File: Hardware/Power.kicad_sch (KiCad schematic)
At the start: 17 parts

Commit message: Replaced the ISOW1044 CAN Transceiver with the ISO1042 + isolated DC-DC and LDO
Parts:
- renumbered C12 to C10, C14 to C11, C16 to C12, C10 to C13, C13 to C14, C17 to C16, C11 to C17
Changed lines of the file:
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@@
 		(on_board yes)
 		(dnp no)
-		(property "Reference" "C14"
+		(property "Reference" "C11"
 			(at 88.9 45.8469 0)
 			(effects
@@
 			(project "CANIO-Board"
 				(path "/a11f98b2-3b09-4cf9-8535-19e509fe91b9/689b7a23-36b5-40a7-9bc7-70c150316ec6"
-					(reference "C14")
+					(reference "C11")
 					(unit 1)
 				)
@@
 		(on_board yes)
 		(dnp no)
-		(property "Reference" "C10"
+		(property "Reference" "C13"
 			(at 27.94 48.3869 0)
 			(effects
@@
 			(project "CANIO-Board"
 				(path "/a11f98b2-3b09-4cf9-8535-19e509fe91b9/689b7a23-36b5-40a7-9bc7-70c150316ec6"
-					(reference "C10")
+					(reference "C13")
 					(unit 1)
 				)
@@
 		(dnp no)
 		(fields_autoplaced yes)
-		(property "Reference" "#PWR09"
+		(property "Reference" "#PWR08"
 			(at 57.15 105.41 0)
 			(effects
@@
 			(project "CANIO-Board"
 				(path "/a11f98b2-3b09-4cf9-8535-19e509fe91b9/689b7a23-36b5-40a7-9bc7-70c150316ec6"
-					(reference "#PWR09")
+					(reference "#PWR08")
 					(unit 1)
 				)
@@
 		(dnp no)
 		(fields_autoplaced yes)
-		(property "Reference" "#FLG03"
+		(property "Reference" "#FLG01"
 			(at 96.52 36.195 0)
 			(effects
@@
 			(project ""
 				(path "/a11f98b2-3b09-4cf9-8535-19e509fe91b9/689b7a23-36b5-40a7-9bc7-70c150316ec6"
-					(reference "#FLG03")
+					(reference "#FLG01")
 					(unit 1)
 				)
@@
 		(dnp no)
 		(fields_autoplaced yes)
-		(property "Reference" "#FLG01"
+		(property "Reference" "#FLG03"
 			(at 39.37 99.695 0)
 			(effects
@@
 			(project "CANIO-Board"
 				(path "/a11f98b2-3b09-4cf9-8535-19e509fe91b9/689b7a23-36b5-40a7-9bc7-70c150316ec6"
-					(reference "#FLG01")
+					(reference "#FLG03")
 					(unit 1)
 				)
@@
 		(dnp no)
 		(fields_autoplaced yes)
-		(property "Reference" "#FLG02"
+		(property "Reference" "#FLG04"
 			(at 73.66 100.965 0)
 			(effects
@@
 			(project "CANIO-Board"
 				(path "/a11f98b2-3b09-4cf9-8535-19e509fe91b9/689b7a23-36b5-40a7-9bc7-70c150316ec6"
-					(reference "#FLG02")
+					(reference "#FLG04")
 					(unit 1)
 				)
@@
 		(on_board yes)
 		(dnp no)
-		(property "Reference" "C11"
+		(property "Reference" "C17"
 			(at 27.94 83.9469 0)
 			(effects
@@
 			(project "CANIO-Board"
 				(path "/a11f98b2-3b09-4cf9-8535-19e509fe91b9/689b7a23-36b5-40a7-9bc7-70c150316ec6"
-					(reference "C11")
+					(reference "C17")
 					(unit 1)
 				)
@@
 		(dnp no)
 		(fields_autoplaced yes)
-		(property "Reference" "#FLG04"
+		(property "Reference" "#FLG02"
 			(at 96.52 71.755 0)
 			(effects
@@
 			(project "CANIO-Board"
 				(path "/a11f98b2-3b09-4cf9-8535-19e509fe91b9/689b7a23-36b5-40a7-9bc7-70c150316ec6"
-					(reference "#FLG04")
+					(reference "#FLG02")
 					(unit 1)
 				)
@@
 		(on_board yes)
 		(dnp no)
-		(property "Reference" "C16"
+		(property "Reference" "C12"
 			(at 99.06 45.8469 0)
 			(effects
@@
 			(project "CANIO-Board"
 				(path "/a11f98b2-3b09-4cf9-8535-19e509fe91b9/689b7a23-36b5-40a7-9bc7-70c150316ec6"
-					(reference "C16")
+					(reference "C12")
 					(unit 1)
 				)
@@
 		(dnp no)
 		(fields_autoplaced yes)
-		(property "Reference" "#PWR05"
+		(property "Reference" "#PWR06"
 			(at 36.83 80.01 0)
 			(effects
@@
 			(project "CANIO-Board"
 				(path "/a11f98b2-3b09-4cf9-8535-19e509fe91b9/689b7a23-36b5-40a7-9bc7-70c150316ec6"
-					(reference "#PWR05")
+					(reference "#PWR06")
 					(unit 1)
 				)
@@
 		(dnp no)
 		(fields_autoplaced yes)
-		(property "Reference" "#PWR010"
+		(property "Reference" "#PWR09"
 			(at 73.66 109.22 0)
 			(effects
@@
 			(project "CANIO-Board"
 				(path "/a11f98b2-3b09-4cf9-8535-19e509fe91b9/689b7a23-36b5-40a7-9bc7-70c150316ec6"
-					(reference "#PWR010")
+					(reference "#PWR09")
 					(unit 1)
 				)
@@
 		(on_board yes)
 		(dnp no)
-		(property "Reference" "C12"
+		(property "Reference" "C10"
 			(at 68.58 40.7669 0)
 			(effects
@@
 			(project "CANIO-Board"
 				(path "/a11f98b2-3b09-4cf9-8535-19e509fe91b9/689b7a23-36b5-40a7-9bc7-70c150316ec6"
-					(reference "C12")
+					(reference "C10")
 					(unit 1)
 				)
@@
 		(on_board yes)
 		(dnp no)
-		(property "Reference" "C13"
+		(property "Reference" "C14"
 			(at 68.58 76.3269 0)
 			(effects
@@
 			(project "CANIO-Board"
 				(path "/a11f98b2-3b09-4cf9-8535-19e509fe91b9/689b7a23-36b5-40a7-9bc7-70c150316ec6"
-					(reference "C13")
+					(reference "C14")
 					(unit 1)
 				)
@@
 		(dnp no)
 		(fields_autoplaced yes)
-		(property "Reference" "#PWR08"
+		(property "Reference" "#PWR010"
 			(at 53.34 199.39 0)
 			(effects
@@
 			(project ""
 				(path "/a11f98b2-3b09-4cf9-8535-19e509fe91b9/689b7a23-36b5-40a7-9bc7-70c150316ec6"
-					(reference "#PWR08")
+					(reference "#PWR010")
 					(unit 1)
 				)
@@
 		(dnp no)
 		(fields_autoplaced yes)
-		(property "Reference" "#PWR06"
+		(property "Reference" "#PWR05"
 			(at 49.53 62.23 0)
 			(effects
@@
 			(project ""
 				(path "/a11f98b2-3b09-4cf9-8535-19e509fe91b9/689b7a23-36b5-40a7-9bc7-70c150316ec6"
-					(reference "#PWR06")
+					(reference "#PWR05")
 					(unit 1)
 				)
@@
 		(on_board yes)
 		(dnp no)
-		(property "Reference" "C17"
+		(property "Reference" "C16"
 			(at 99.06 81.4069 0)
 			(effects
@@
 			(project "CANIO-Board"
 				(path "/a11f98b2-3b09-4cf9-8535-19e509fe91b9/689b7a23-36b5-40a7-9bc7-70c150316ec6"
-					(reference "C17")
-					(unit 1)
-				)
+					(reference "C16")
+					(unit 1)
+				)

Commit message: Replaced G0B1KET6 with KET6N in schematic
- Updated the schematic with new symbol and pinout.
- Updated the rest of the schematic with all resulting changes
	- This includes the 8 output channels, 7 GPIOs, and slightly
	  different WAGO connector configuration.
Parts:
- renumbered C10 to C15, C11 to C16, C12 to C17, C13 to C18, C14 to C19, C15 to C20, C16 to C21, C17 to C22, R8 to R11, R9 to R12
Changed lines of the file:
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@@
 		(on_board yes)
 		(dnp no)
-		(property "Reference" "C11"
+		(property "Reference" "C16"
 			(at 88.9 45.8469 0)
 			(effects
@@
 			(project "CANIO-Board"
 				(path "/a11f98b2-3b09-4cf9-8535-19e509fe91b9/689b7a23-36b5-40a7-9bc7-70c150316ec6"
-					(reference "C11")
+					(reference "C16")
 					(unit 1)
 				)
@@
 		(dnp no)
 		(fields_autoplaced yes)
-		(property "Reference" "#PWR04"
+		(property "Reference" "#PWR05"
 			(at 36.83 44.45 0)
 			(effects
@@
 			(project ""
 				(path "/a11f98b2-3b09-4cf9-8535-19e509fe91b9/689b7a23-36b5-40a7-9bc7-70c150316ec6"
-					(reference "#PWR04")
+					(reference "#PWR05")
 					(unit 1)
 				)
@@
 		(on_board yes)
 		(dnp no)
-		(property "Reference" "C13"
+		(property "Reference" "C18"
 			(at 27.94 48.3869 0)
 			(effects
@@
 			(project "CANIO-Board"
 				(path "/a11f98b2-3b09-4cf9-8535-19e509fe91b9/689b7a23-36b5-40a7-9bc7-70c150316ec6"
-					(reference "C13")
+					(reference "C18")
 					(unit 1)
 				)
@@
 		(dnp no)
 		(fields_autoplaced yes)
-		(property "Reference" "R9"
+		(property "Reference" "R12"
 			(at 77.47 184.15 90)
 			(effects
@@
 			(project "CANIO-Board"
 				(path "/a11f98b2-3b09-4cf9-8535-19e509fe91b9/689b7a23-36b5-40a7-9bc7-70c150316ec6"
-					(reference "R9")
+					(reference "R12")
 					(unit 1)
 				)
@@
 		(dnp no)
 		(fields_autoplaced yes)
-		(property "Reference" "#PWR08"
+		(property "Reference" "#PWR09"
 			(at 57.15 105.41 0)
 			(effects
@@
 			(project "CANIO-Board"
 				(path "/a11f98b2-3b09-4cf9-8535-19e509fe91b9/689b7a23-36b5-40a7-9bc7-70c150316ec6"
-					(reference "#PWR08")
+					(reference "#PWR09")
 					(unit 1)
 				)
@@
 		(dnp no)
 		(fields_autoplaced yes)
-		(property "Reference" "#PWR07"
+		(property "Reference" "#PWR08"
 			(at 49.53 97.79 0)
 			(effects
@@
 			(project "CANIO-Board"
 				(path "/a11f98b2-3b09-4cf9-8535-19e509fe91b9/689b7a23-36b5-40a7-9bc7-70c150316ec6"
-					(reference "#PWR07")
+					(reference "#PWR08")
 					(unit 1)
 				)
@@
 		(on_board yes)
 		(dnp no)
-		(property "Reference" "C17"
+		(property "Reference" "C22"
 			(at 27.94 83.9469 0)
 			(effects
@@
 			(project "CANIO-Board"
 				(path "/a11f98b2-3b09-4cf9-8535-19e509fe91b9/689b7a23-36b5-40a7-9bc7-70c150316ec6"
-					(reference "C17")
+					(reference "C22")
 					(unit 1)
 				)
@@
 		(on_board yes)
 		(dnp no)
-		(property "Reference" "C12"
+		(property "Reference" "C17"
 			(at 99.06 45.8469 0)
 			(effects
@@
 			(project "CANIO-Board"
 				(path "/a11f98b2-3b09-4cf9-8535-19e509fe91b9/689b7a23-36b5-40a7-9bc7-70c150316ec6"
-					(reference "C12")
+					(reference "C17")
 					(unit 1)
 				)
@@
 		(dnp no)
 		(fields_autoplaced yes)
-		(property "Reference" "#PWR06"
+		(property "Reference" "#PWR07"
 			(at 36.83 80.01 0)
 			(effects
@@
 			(project "CANIO-Board"
 				(path "/a11f98b2-3b09-4cf9-8535-19e509fe91b9/689b7a23-36b5-40a7-9bc7-70c150316ec6"
-					(reference "#PWR06")
+					(reference "#PWR07")
 					(unit 1)
 				)
@@
 		(dnp no)
 		(fields_autoplaced yes)
-		(property "Reference" "#PWR09"
+		(property "Reference" "#PWR010"
 			(at 73.66 109.22 0)
 			(effects
@@
 			(project "CANIO-Board"
 				(path "/a11f98b2-3b09-4cf9-8535-19e509fe91b9/689b7a23-36b5-40a7-9bc7-70c150316ec6"
-					(reference "#PWR09")
+					(reference "#PWR010")
 					(unit 1)
 				)
@@
 		(on_board yes)
 		(dnp no)
-		(property "Reference" "C10"
+		(property "Reference" "C15"
 			(at 68.58 40.7669 0)
 			(effects
@@
 			(project "CANIO-Board"
 				(path "/a11f98b2-3b09-4cf9-8535-19e509fe91b9/689b7a23-36b5-40a7-9bc7-70c150316ec6"
-					(reference "C10")
+					(reference "C15")
 					(unit 1)
 				)
@@
 		(on_board yes)
 		(dnp no)
-		(property "Reference" "C14"
+		(property "Reference" "C19"
 			(at 68.58 76.3269 0)
 			(effects
@@
 			(project "CANIO-Board"
 				(path "/a11f98b2-3b09-4cf9-8535-19e509fe91b9/689b7a23-36b5-40a7-9bc7-70c150316ec6"
-					(reference "C14")
+					(reference "C19")
 					(unit 1)
 				)
@@
 		(dnp no)
 		(fields_autoplaced yes)
-		(property "Reference" "#PWR010"
+		(property "Reference" "#PWR011"
 			(at 53.34 199.39 0)
 			(effects
@@
 			(project ""
 				(path "/a11f98b2-3b09-4cf9-8535-19e509fe91b9/689b7a23-36b5-40a7-9bc7-70c150316ec6"
-					(reference "#PWR010")
+					(reference "#PWR011")
 					(unit 1)
 				)
@@
 		(dnp no)
 		(fields_autoplaced yes)
-		(property "Reference" "#PWR05"
+		(property "Reference" "#PWR06"
 			(at 49.53 62.23 0)
 			(effects
@@
 			(project ""
 				(path "/a11f98b2-3b09-4cf9-8535-19e509fe91b9/689b7a23-36b5-40a7-9bc7-70c150316ec6"
-					(reference "#PWR05")
+					(reference "#PWR06")
 					(unit 1)
 				)
@@
 		(dnp no)
 		(fields_autoplaced yes)
-		(property "Reference" "R8"
+		(property "Reference" "R11"
 			(at 35.56 184.15 90)
 			(effects
@@
 			(project ""
 				(path "/a11f98b2-3b09-4cf9-8535-19e509fe91b9/689b7a23-36b5-40a7-9bc7-70c150316ec6"
-					(reference "R8")
+					(reference "R11")
 					(unit 1)
 				)
@@
 		(on_board yes)
 		(dnp no)
-		(property "Reference" "C16"
+		(property "Reference" "C21"
 			(at 99.06 81.4069 0)
 			(effects
@@
 			(project "CANIO-Board"
 				(path "/a11f98b2-3b09-4cf9-8535-19e509fe91b9/689b7a23-36b5-40a7-9bc7-70c150316ec6"
-					(reference "C16")
+					(reference "C21")
 					(unit 1)
 				)
@@
 		(on_board yes)
 		(dnp no)
-		(property "Reference" "C15"
+		(property "Reference" "C20"
 			(at 88.9 81.4069 0)
 			(effects
@@
 			(project "CANIO-Board"
 				(path "/a11f98b2-3b09-4cf9-8535-19e509fe91b9/689b7a23-36b5-40a7-9bc7-70c150316ec6"
-					(reference "C15")
+					(reference "C20")
 					(unit 1)
 				)
@@
 		(dnp no)
 		(fields_autoplaced yes)
-		(property "Reference" "#PWR011"
+		(property "Reference" "#PWR012"
 			(at 95.25 199.39 0)
 			(effects
@@
 			(project "CANIO-Board"
 				(path "/a11f98b2-3b09-4cf9-8535-19e509fe91b9/689b7a23-36b5-40a7-9bc7-70c150316ec6"
-					(reference "#PWR011")
-					(unit 1)
-				)
+					(reference "#PWR012")
+					(unit 1)
+				)

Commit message: Replaced buck converters with drop in replacements
Co-authored-by: Kostadin Madjovski <155325994+bivein@users.noreply.github.com>
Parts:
- BUCK1: value AP63203WU -> AP63203QWU-7
- BUCK2: value AP63205WU -> AP63205QWU-7
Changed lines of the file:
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@@
 			)
 		)
-		(property "Value" "AP63203WU"
+		(property "Value" "AP63203QWU-7"
 			(at 49.53 38.1 0)
 			(effects
@@
 			)
 		)
-		(property "Value" "AP63205WU"
+		(property "Value" "AP63205QWU-7"
 			(at 49.53 73.66 0)
 			(effects

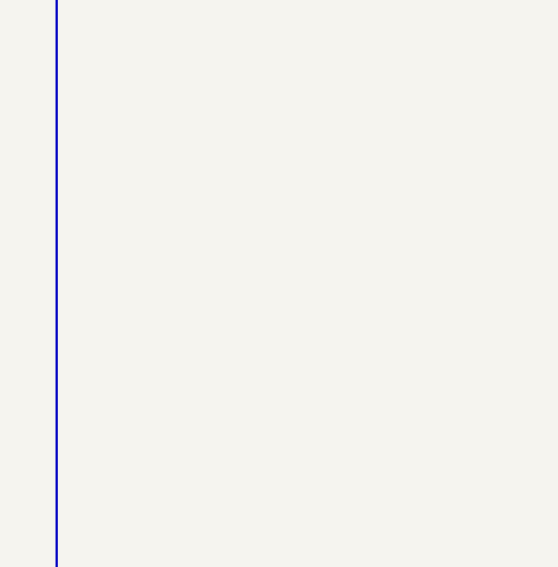
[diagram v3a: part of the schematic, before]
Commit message: Finished the board
- Board layout and routing is finished. Need to fix ~30 ERC errors and
  add thorough notes throughout, but otherwise that's it.
- Once ERC errors are resolved, will post BOM and Gerbers as a release.
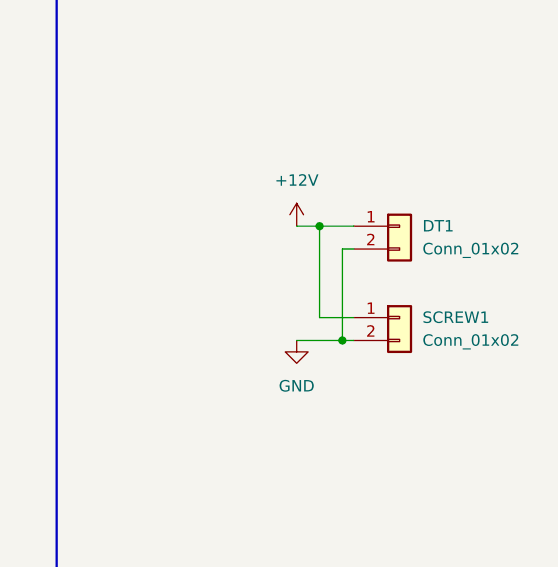
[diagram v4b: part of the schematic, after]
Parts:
- added DT1: Conn_01x02, footprints:TE_DTF13-2P, symbol Connector_Generic:Conn_01x02
- added SCREW1: Conn_01x02, TerminalBlock:TerminalBlock_MaiXu_MX126-5.0-02P_1x02_P5.00mm, symbol Connector_Generic:Conn_01x02
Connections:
- net +12V: now also DT1.1 (Pin_1), SCREW1.1 (Pin_1)
- net GND: now also DT1.2 (Pin_2), SCREW1.2 (Pin_2)

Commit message: final changes on pcb
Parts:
- added D1: D, Diode_SMD:D_SMC_Handsoldering, symbol Device:D
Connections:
- net +12V: now also D1.1 (K); no longer DT1.1 (Pin_1), SCREW1.1 (Pin_1)
- new net Raw12V: D1.2 (A), DT1.1 (Pin_1), SCREW1.1 (Pin_1)
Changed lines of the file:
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@@
+	(wire
+		(pts
+			(xy 130.81 45.72) (xy 133.35 45.72)
+		)
+		(stroke
+			(width 0)
+			(type default)
+		)
+	)
+	(wire
+		(pts
+			(xy 143.51 39.37) (xy 153.67 39.37)
+		)
+		(stroke
+			(width 0)
+			(type default)
+		)
+	)
 	(wire
 		(pts
@@
 		(pts
 			(xy 53.34 190.5) (xy 53.34 193.04)
+		)
+		(stroke
+			(width 0)
+			(type default)
+		)
+	)
+	(wire
+		(pts
+			(xy 143.51 45.72) (xy 143.51 39.37)
 		)
 		(stroke
@@
 		)
 	)
+	(label "Raw12V"
+		(at 153.67 39.37 180)
+		(effects
+			(font
+				(size 1.27 1.27)
+			)
+			(justify right bottom)
+		)
+	)
 	(global_label "5v0"
 		(shape input)
@@
 	(symbol
 		(lib_id "power:+12V")
-		(at 140.97 45.72 0)
+		(at 130.81 45.72 0)
 		(unit 1)
 		(exclude_from_sim no)
@@
 		(fields_autoplaced yes)
 		(property "Reference" "#PWR06"
-			(at 140.97 49.53 0)
+			(at 130.81 49.53 0)
 			(effects
 				(font
@@
 		)
 		(property "Value" "+12V"
-			(at 140.97 40.64 0)
+			(at 130.81 40.64 0)
 			(effects
 				(font
@@
 		)
 		(property "Footprint" ""
-			(at 140.97 45.72 0)
+			(at 130.81 45.72 0)
 			(effects
 				(font
@@
 		)
 		(property "Datasheet" ""
-			(at 140.97 45.72 0)
+			(at 130.81 45.72 0)
 			(effects
 				(font
@@
 		)
 		(property "Description" "Power symbol creates a global label with name \"+12V\""
-			(at 140.97 45.72 0)
+			(at 130.81 45.72 0)
 			(effects
 				(font
@@
 					(unit 1)
 				)
+			)
+		)
+	)
+	(symbol
+		(lib_id "Device:D")
+		(at 137.16 45.72 0)
+		(unit 1)
+		(exclude_from_sim no)
+		(in_bom yes)
+		(on_board yes)
+		(dnp no)
+		(fields_autoplaced yes)
+		(property "Reference" "D1"
+			(at 137.16 39.37 0)
+			(effects
+				(font
+					(size 1.27 1.27)
+				)
+			)
+		)
+		(property "Value" "D"
+			(at 137.16 41.91 0)
+			(effects
+				(font
+					(size 1.27 1.27)
+				)
+			)
+		)
+		(property "Footprint" "Diode_SMD:D_SMC_Handsoldering"
+			(at 137.16 45.72 0)
+			(effects
+				(font
+					(size 1.27 1.27)
+				)
+				(hide yes)
+			)
+		)
+		(property "Datasheet" "~"
+			(at 137.16 45.72 0)
+			(effects
+				(font
+					(size 1.27 1.27)
+				)
+				(hide yes)
+			)
+		)
+		(property "Description" "Diode"
+			(at 137.16 45.72 0)
+			(effects
+				(font
+					(size 1.27 1.27)
+				)
+				(hide yes)
+			)
+		)
+		(property "Sim.Device" "D"
+			(at 137.16 45.72 0)
+			(effects
+				(font
+					(size 1.27 1.27)
+				)
+				(hide yes)
+			)
+		)
+		(property "Sim.Pins" "1=K 2=A"
+			(at 137.16 45.72 0)
+			(effects
+				(font
+					(size 1.27 1.27)
+				)
+				(hide yes)
+			)
+		)
+		(pin "2"
+		)
+		(pin "1"
+		)
+		(instances
+			(project ""
+				(path "/a11f98b2-3b09-4cf9-8535-19e509fe91b9/689b7a23-36b5-40a7-9bc7-70c150316ec6"
+					(reference "D1")
+					(unit 1)
+				)
